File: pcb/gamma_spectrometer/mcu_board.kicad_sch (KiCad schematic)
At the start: 39 parts, among them U301 REF35250QDBVR, U302 STM32G474MET6, U303 W25Q64JVSSIQ, Y301 ABM8G-16.000MHZ-4Y-T3

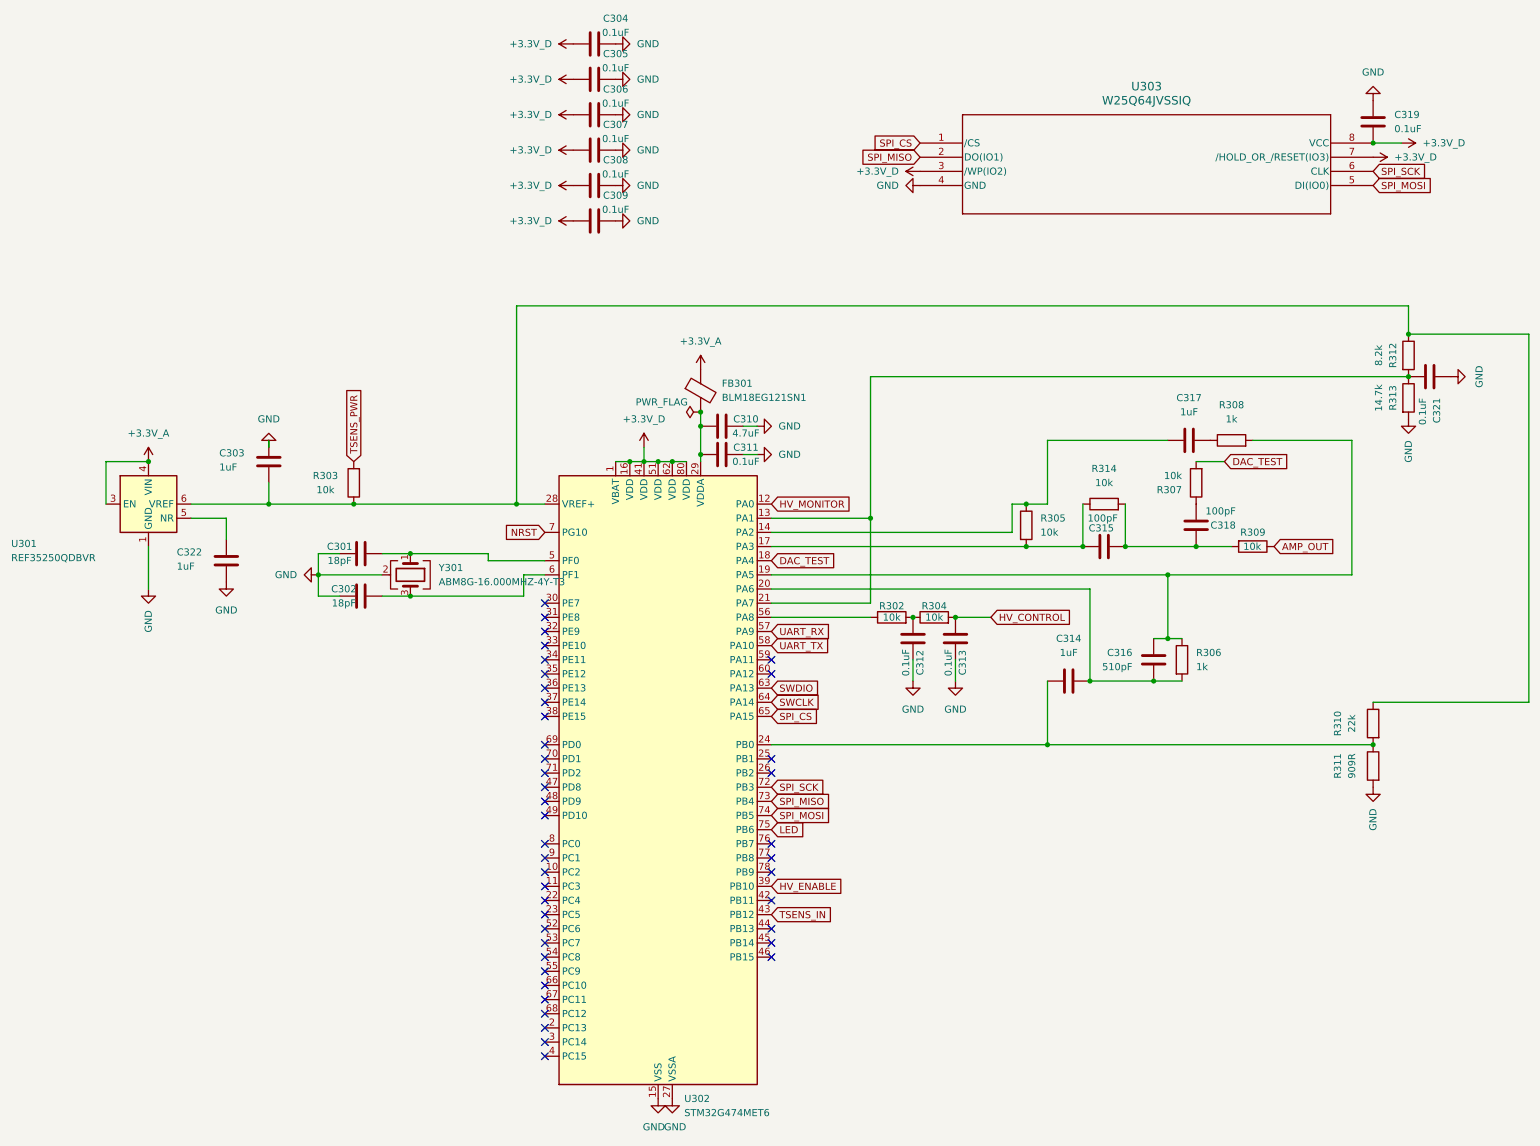
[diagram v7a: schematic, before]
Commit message: pcb: плата МК на LQFP-48 (STM32G474CBT6), герберы перевыгружены
Схема и плата МК переразведены под STM32G474CBT6 в LQFP-48 7x7 вместо
STM32G474MET6 в LQFP-80 12x12. Заказ MCT6TR отменён поставщиком из-за
пересорта; CBT6 есть в наличии за 238 руб против 1410 и 6 недель.
Все 24 задействованных вывода есть и в LQFP-48.

Снесены 289 дорожек и 127 виа в круге (195, 100) R22.5, разведено заново.
Удалены C304 и C309 — лишние пары развязки (выводов питания стало 4 из 6).
Падам VSSA/VSS 19/23/35/47 выставлено zone_connect = 2: при шаге 0.5 мм
два мостика терморазгрузки не влезают, сплошное соединение заодно даёт
минимальную индуктивность возврата.

Контур заготовки не менялся: Edge_Cuts байт в байт как в версии, по которой
выставлен счёт N 19696. Сверловка плат USB, ВВ и делителя идентична прежней.
Компонентов 178 -> 176, цепей 118 без изменений, ERC 0 ошибок.

Попутно закрыто:
- 5 виа с пояском 0.15 мм. Корень не в разводке, а в настройке проекта:
  класс Default держал via_diameter = 0.6, а min_via_annular_width = 0.1,
  поэтому каждая новая виа выходила бракованной молча. Теперь 0.8 и 0.25.
- Плата МК потеряла посадочное место стоек STANDOFF_M2.5_GND_x3_TRIANGLE
  (три отверстия D2.8 крепления стека) — оно стоит ровно в центре и ушло
  вместе с выделением при сносе разводки. Нашлось сравнением сверловки
  по платам: D2.80 было 12, стало 9. Восстановлено из HEAD байт в байт.
- Замыкание GND на UART_TX — следствие предыдущего: пока стоек не было,
  дорожка на B.Cu легла через их пад на 330 градусах.
- Оторванный остров заливки под R311: нижнее плечо делителя PGA x4 было
  фактически не заземлено.
- Разрыв дорожки у C18a201 на плате ВВ (ВЧ-фильтр выхода был разомкнут).
- Дублирующая дорожка +3.3V_D на плате USB.

DRC: 413 нарушений, по делу 3 принятых ВВ-правила. Замыканий, мостиков
маски, висячих дорожек и неполных терморазгрузок 0. Не соединено 26 =
25 межплатных (мост — цанг-пины в стеке) + одна старая пара зон на USB.
Виа 210, поясок 0.250 у всех. Сверловка сверена с пла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
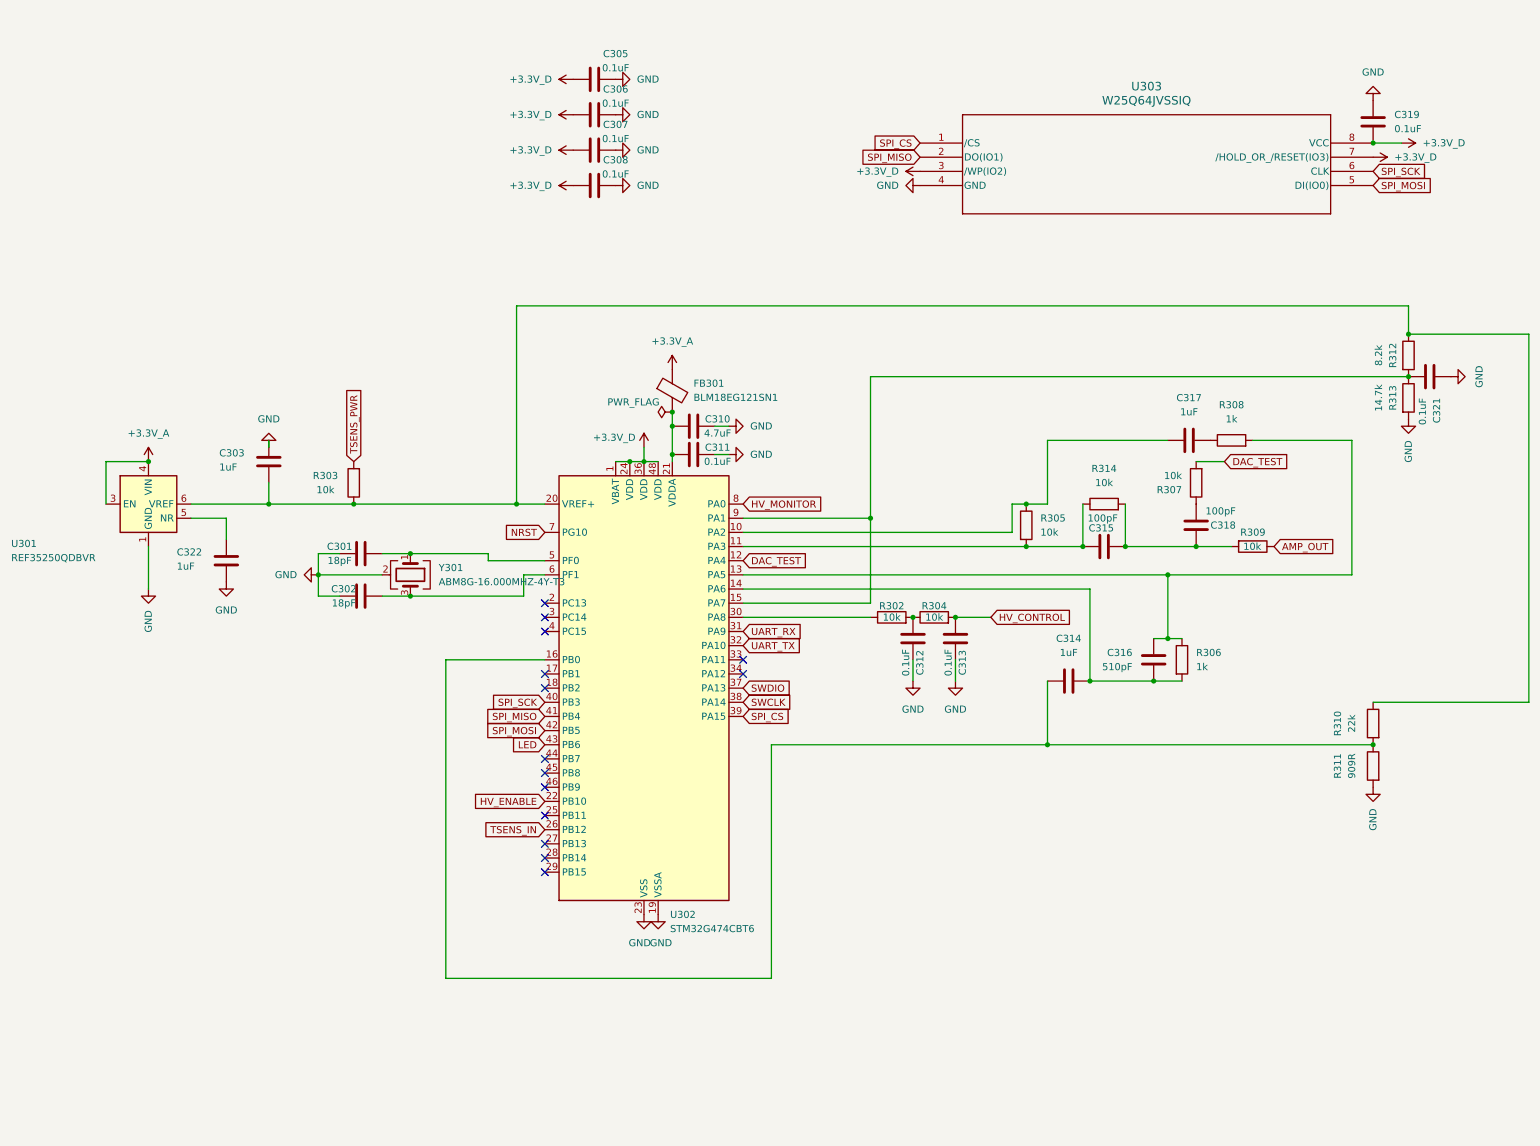
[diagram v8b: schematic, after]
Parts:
- removed C304, C309: 0.1uF, Capacitor_SMD:C_0603_1608Metric_Pad1.08x0.95mm_HandSolder, symbol Device:C
- U302: value STM32G474MET6 -> STM32G474CBT6; footprint Package_QFP:LQFP-80_12x12mm_P0.5mm -> Package_QFP:LQFP-48_7x7mm_P0.5mm; symbol MCU_ST_STM32G4:STM32G474METx -> MCU_ST_STM32G4:STM32G474CBTx; PN STM32G474MET6 -> STM32G474CBT6; Ссылка на покупку  https://www.electronshik.ru/item/ST/STM32G474MET6 -> https://www.electronshik.ru/item/ST/STM32G474CBT6
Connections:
- net +3.3V_D: now also U302.24 (VDD), U302.36 (VDD), U302.48 (VDD); no longer U302.16 (VDD), U302.41 (VDD), U302.51 (VDD), U302.62 (VDD), U302.80 (VDD)
- net DAC_TEST: now also U302.12 (PA4); no longer U302.18 (PA4)
- net GND: now also U302.19 (VSSA), U302.23 (VSS), U302.35 (VSS), U302.47 (VSS); no longer U302.15 (VSS), U302.27 (VSSA), U302.40 (VSS), U302.50 (VSS), U302.61 (VSS), U302.79 (VSS)
- net HV_ENABLE: now also U302.22 (PB10); no longer U302.39 (PB10)
- net HV_MONITOR: now also U302.8 (PA0); no longer U302.12 (PA0)
- net LED: now also U302.43 (PB6); no longer U302.75 (PB6)
- net SPI_CS: now also U302.39 (PA15); no longer U302.65 (PA15)
- net SPI_MISO: now also U302.41 (PB4); no longer U302.73 (PB4)
- net SPI_MOSI: now also U302.42 (PB5); no longer U302.74 (PB5)
- net SPI_SCK: now also U302.40 (PB3); no longer U302.72 (PB3)
- net SWCLK: now also U302.38 (PA14); no longer U302.64 (PA14)
- net SWDIO: now also U302.37 (PA13); no longer U302.63 (PA13)
- net TSENS_IN: now also U302.26 (PB12); no longer U302.43 (PB12)
- net UART_RX: now also U302.31 (PA9); no longer U302.57 (PA9)
- net UART_TX: now also U302.32 (PA10); no longer U302.58 (PA10)
- net at C315.2, R305.2, R314.1: now also U302.11 (PA3); no longer U302.17 (PA3)
- net at C310.1, C311.1, FB301.2: now also U302.21 (VDDA); no longer U302.29 (VDDA)
- net at C314.1, R310.2, R311.1: now also U302.16 (PB0); no longer U302.24 (PB0)
- net at C314.2, C316.2, R306.2: now also U302.14 (PA6); no longer U302.20 (PA6)
- net at C303.2, R303.1, R310.1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: now also U302.20 (VREF+); no longer U302.28 (VREF+)
- net at C321.2, R312.2, R313.1: now also U302.15 (PA7), U302.9 (PA1); no longer U302.13 (PA1), U302.21 (PA7)
- net at C317.1, R305.1: now also U302.10 (PA2); no longer U302.14 (PA2)
- net at C316.1, R306.1, R308.2: now also U302.13 (PA5); no longer U302.19 (PA5)
- net at R302.1: now also U302.30 (PA8); no longer U302.56 (PA8)
- no-connect marks 42 -> 14
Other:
- moved on the sheet: C310, C311, FB301
